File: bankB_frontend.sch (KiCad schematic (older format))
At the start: 2 parts

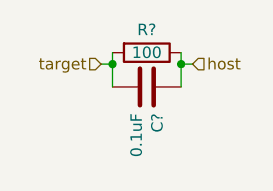
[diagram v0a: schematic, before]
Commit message: Completed routing of new connectors.
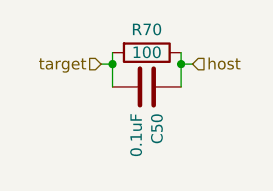
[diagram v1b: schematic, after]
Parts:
- gave numbers to parts that had none: 2
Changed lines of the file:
@@
 $Descr A4 11693 8268
 encoding utf-8
-Sheet 10 10
+Sheet 13 17
 Title ""
 Date ""
@@
 P 4950 4750
 AR Path="/5D737602" Ref="C?"  Part="1"
-AR Path="/5D737162/5D737602" Ref="C?"  Part="1"
+AR Path="/5D737162/5D737602" Ref="C17"  Part="1"
 AR Path="/5D7D27C1/5D737602" Ref="C?"  Part="1"
 AR Path="/5D805C30/5D737602" Ref="C?"  Part="1"
@@
 AR Path="/5D8D3452/5D737602" Ref="C?"  Part="1"
 AR Path="/5D9068C1/5D737602" Ref="C?"  Part="1"
-AR Path="/5D96E70D/5D737602" Ref="C?"  Part="1"
-AR Path="/5D9A1BDE/5D737602" Ref="C?"  Part="1"
-AR Path="/5D9A1BE2/5D737602" Ref="C?"  Part="1"
-AR Path="/5D9D50BB/5D737602" Ref="C?"  Part="1"
-AR Path="/5D9D50BF/5D737602" Ref="C?"  Part="1"
-AR Path="/5D9D50C3/5D737602" Ref="C?"  Part="1"
-AR Path="/5D9D50C7/5D737602" Ref="C?"  Part="1"
-F 0 "C?" H 5065 4796 50  0000 L CNN
+AR Path="/5D96E70D/5D737602" Ref="C44"  Part="1"
+AR Path="/5D9A1BDE/5D737602" Ref="C45"  Part="1"
+AR Path="/5D9A1BE2/5D737602" Ref="C46"  Part="1"
+AR Path="/5D9D50BB/5D737602" Ref="C47"  Part="1"
+AR Path="/5D9D50BF/5D737602" Ref="C48"  Part="1"
+AR Path="/5D9D50C3/5D737602" Ref="C49"  Part="1"
+AR Path="/5D9D50C7/5D737602" Ref="C50"  Part="1"
+F 0 "C50" H 5065 4796 50  0000 L CNN
 F 1 "0.1uF" H 5065 4705 50  0000 L CNN
 F 2 "gsg-modules:0402" H 4988 4600 50  0001 C CNN
@@
 P 4950 4600
 AR Path="/5D73760C" Ref="R?"  Part="1"
-AR Path="/5D737162/5D73760C" Ref="R?"  Part="1"
+AR Path="/5D737162/5D73760C" Ref="R10"  Part="1"
 AR Path="/5D7D27C1/5D73760C" Ref="R?"  Part="1"
 AR Path="/5D805C30/5D73760C" Ref="R?"  Part="1"
@@
 AR Path="/5D8D3452/5D73760C" Ref="R?"  Part="1"
 AR Path="/5D9068C1/5D73760C" Ref="R?"  Part="1"
-AR Path="/5D96E70D/5D73760C" Ref="R?"  Part="1"
-AR Path="/5D9A1BDE/5D73760C" Ref="R?"  Part="1"
-AR Path="/5D9A1BE2/5D73760C" Ref="R?"  Part="1"
-AR Path="/5D9D50BB/5D73760C" Ref="R?"  Part="1"
-AR Path="/5D9D50BF/5D73760C" Ref="R?"  Part="1"
-AR Path="/5D9D50C3/5D73760C" Ref="R?"  Part="1"
-AR Path="/5D9D50C7/5D73760C" Ref="R?"  Part="1"
-F 0 "R?" V 4850 4600 50  0000 C CNN
+AR Path="/5D96E70D/5D73760C" Ref="R64"  Part="1"
+AR Path="/5D9A1BDE/5D73760C" Ref="R65"  Part="1"
+AR Path="/5D9A1BE2/5D73760C" Ref="R66"  Part="1"
+AR Path="/5D9D50BB/5D73760C" Ref="R67"  Part="1"
+AR Path="/5D9D50BF/5D73760C" Ref="R68"  Part="1"
+AR Path="/5D9D50C3/5D73760C" Ref="R69"  Part="1"
+AR Path="/5D9D50C7/5D73760C" Ref="R70"  Part="1"
+F 0 "R70" V 4850 4600 50  0000 C CNN
 F 1 "100" V 4950 4600 50  0000 C CNN
 F 2 "gsg-modules:0402" V 4880 4600 50  0001 C CNN

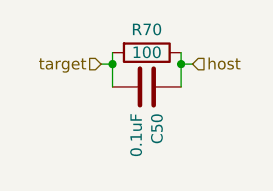
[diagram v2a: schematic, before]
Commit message: schematic: cleanup and squish onto a page
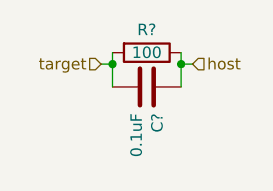
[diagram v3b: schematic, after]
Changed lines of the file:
@@
 EESchema Schematic File Version 4
 LIBS:foxglove-cache
-EELAYER 26 0
+EELAYER 29 0
 EELAYER END
 $Descr A4 11693 8268
 encoding utf-8
-Sheet 10 17
+Sheet 2 17
 Title ""
 Date ""
@@
 AR Path="/5D9D50C3/5D737602" Ref="C49"  Part="1"
 AR Path="/5D9D50C7/5D737602" Ref="C50"  Part="1"
-F 0 "C50" H 5065 4796 50  0000 L CNN
+F 0 "C?" H 5065 4796 50  0000 L CNN
 F 1 "0.1uF" H 5065 4705 50  0000 L CNN
 F 2 "gsg-modules:0402" H 4988 4600 50  0001 C CNN
@@
 AR Path="/5D9D50C3/5D73760C" Ref="R69"  Part="1"
 AR Path="/5D9D50C7/5D73760C" Ref="R70"  Part="1"
-F 0 "R70" V 4850 4600 50  0000 C CNN
+F 0 "R?" V 4850 4600 50  0000 C CNN
 F 1 "100" V 4950 4600 50  0000 C CNN
 F 2 "gsg-modules:0402" V 4880 4600 50  0001 C CNN
